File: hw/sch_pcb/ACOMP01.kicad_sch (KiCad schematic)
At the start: 20 parts, among them IC1 TLV3604DCKR, IC2 LMH7220MK_NOPB, J1 Umin ... Umax, J2 Conn_Coaxial, J3 Conn_Coaxial, J4 Conn_Coaxial, J5 Conn_Coaxial, J6 HEADER_2x04_PARALLEL, J7 HEADER_2x04_PARALLEL, M1 HOLE M3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

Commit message: pcb layout
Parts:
- C2: value 100nF -> 1uF
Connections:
- net OUT+_LMH renamed LMH_OUT+
- net OUT+_TLV renamed TLV_OUT+
- net OUT-_LMH renamed LMH_OUT-
- net OUT-_TLV renamed TLV_OUT-
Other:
- note added: "2.4 - 5.5 V"
- note added: "2.7 - 12 V"
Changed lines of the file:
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@@
+    (effects (font (size 1.524 1.524)) (justify left bottom))
+  )
+  (text "2.4 - 5.5 V" (at 102.87 81.28 0)
     (effects (font (size 1.524 1.524)) (justify left bottom))
   )
@@
     (effects (font (size 1.524 1.524)) (justify left bottom))
   )
-  (label "OUT+_TLV" (at 163.83 68.58 180)
+  (text "2.7 - 12 V" (at 102.87 115.57 0)
+    (effects (font (size 1.524 1.524)) (justify left bottom))
+  )
+  (label "IN+_LMH" (at 52.07 106.68 0)
+    (effects (font (size 1.524 1.524)) (justify left bottom))
+  )
+  (label "LMH_OUT+" (at 163.83 100.33 180)
     (effects (font (size 1.524 1.524)) (justify right bottom))
   )
-  (label "OUT-_TLV" (at 129.54 68.58 0)
-    (effects (font (size 1.524 1.524)) (justify left bottom))
-  )
-  (label "IN+_LMH" (at 52.07 106.68 0)
-    (effects (font (size 1.524 1.524)) (justify left bottom))
-  )
   (label "IN+_TLV" (at 52.07 58.42 0)
     (effects (font (size 1.524 1.524)) (justify left bottom))
-  )
-  (label "OUT-_LMH" (at 163.83 113.03 180)
-    (effects (font (size 1.524 1.524)) (justify right bottom))
   )
   (label "IN-_TLV" (at 129.54 77.47 0)
@@
     (effects (font (size 1.524 1.524)) (justify right bottom))
   )
-  (label "OUT-_TLV" (at 163.83 81.28 180)
+  (label "IN-_TLV" (at 52.07 74.93 0)
+    (effects (font (size 1.524 1.524)) (justify left bottom))
+  )
+  (label "LMH_OUT-" (at 163.83 113.03 180)
     (effects (font (size 1.524 1.524)) (justify right bottom))
   )
-  (label "IN-_TLV" (at 52.07 74.93 0)
-    (effects (font (size 1.524 1.524)) (justify left bottom))
-  )
-  (label "OUT+_LMH" (at 128.27 113.03 0)
-    (effects (font (size 1.524 1.524)) (justify left bottom))
-  )
-  (label "OUT-_LMH" (at 90.17 113.03 180)
-    (effects (font (size 1.524 1.524)) (justify right bottom))
+  (label "LMH_OUT+" (at 128.27 113.03 0)
+    (effects (font (size 1.524 1.524)) (justify left bottom))
   )
   (label "IN-_LMH" (at 52.07 123.19 0)
     (effects (font (size 1.524 1.524)) (justify left bottom))
-  )
-  (label "OUT+_TLV" (at 88.9 68.58 180)
-    (effects (font (size 1.524 1.524)) (justify right bottom))
   )
   (label "IN+_LMH" (at 128.27 105.41 0)
@@
     (effects (font (size 1.524 1.524)) (justify right bottom))
   )
-  (label "OUT+_LMH" (at 163.83 100.33 180)
+  (label "TLV_OUT+" (at 88.9 68.58 180)
     (effects (font (size 1.524 1.524)) (justify right bottom))
+  )
+  (label "TLV_OUT-" (at 163.83 81.28 180)
+    (effects (font (size 1.524 1.524)) (justify right bottom))
+  )
+  (label "TLV_OUT+" (at 163.83 68.58 180)
+    (effects (font (size 1.524 1.524)) (justify right bottom))
+  )
+  (label "LMH_OUT-" (at 90.17 113.03 180)
+    (effects (font (size 1.524 1.524)) (justify right bottom))
+  )
+  (label "TLV_OUT-" (at 129.54 68.58 0)
+    (effects (font (size 1.524 1.524)) (justify left bottom))
   )
   (symbol (lib_id "header:HEADER_2x03_PARALLEL") (at 267.97 26.67 0) (unit 1)
@@
       (effects (font (size 1.27 1.27)) (justify left))
     )
-    (property "Value" "100nF" (id 1) (at 246.38 34.29 0)
+    (property "Value" "1uF" (id 1) (at 246.38 34.29 0)
       (effects (font (size 1.27 1.27)) (justify left))
     )
@@
     )
     (path "/7fab2e4e-c967-46aa-8b62-a4eb722fba85"
-      (reference "C2") (unit 1) (value "100nF") (footprint "Capacitor_SMD:C_0805_2012Metric")
+      (reference "C2") (unit 1) (value "1uF") (footprint "Capacitor_SMD:C_0805_2012Metric")
     )
     (path "/f66f54fb-1d0d-47f4-b95c-230a639b65a5"

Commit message: Cleanup of some DRC errors.
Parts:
- J1: value Umin ... Umax -> 2,4 - 5,5V
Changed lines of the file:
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@@
       (effects (font (size 1.524 1.524)))
     )
-    (property "Value" "Umin ... Umax" (id 1) (at 267.97 21.59 0)
+    (property "Value" "2,4 - 5,5V" (id 1) (at 267.97 21.59 0)
       (effects (font (size 1.524 1.524)))
     )
@@
     )
     (path "/00000000-0000-0000-0000-0000549d65bc"
-      (reference "J1") (unit 1) (value "Umin ... Umax") (footprint "Mlab_Pin_Headers:Straight_2x03")
+      (reference "J1") (unit 1) (value "2,4 - 5,5V") (footprint "Mlab_Pin_Headers:Straight_2x03")
     )
     (path "/b19fad9a-d3d5-4b48-b6c5-b8fa621dea36"

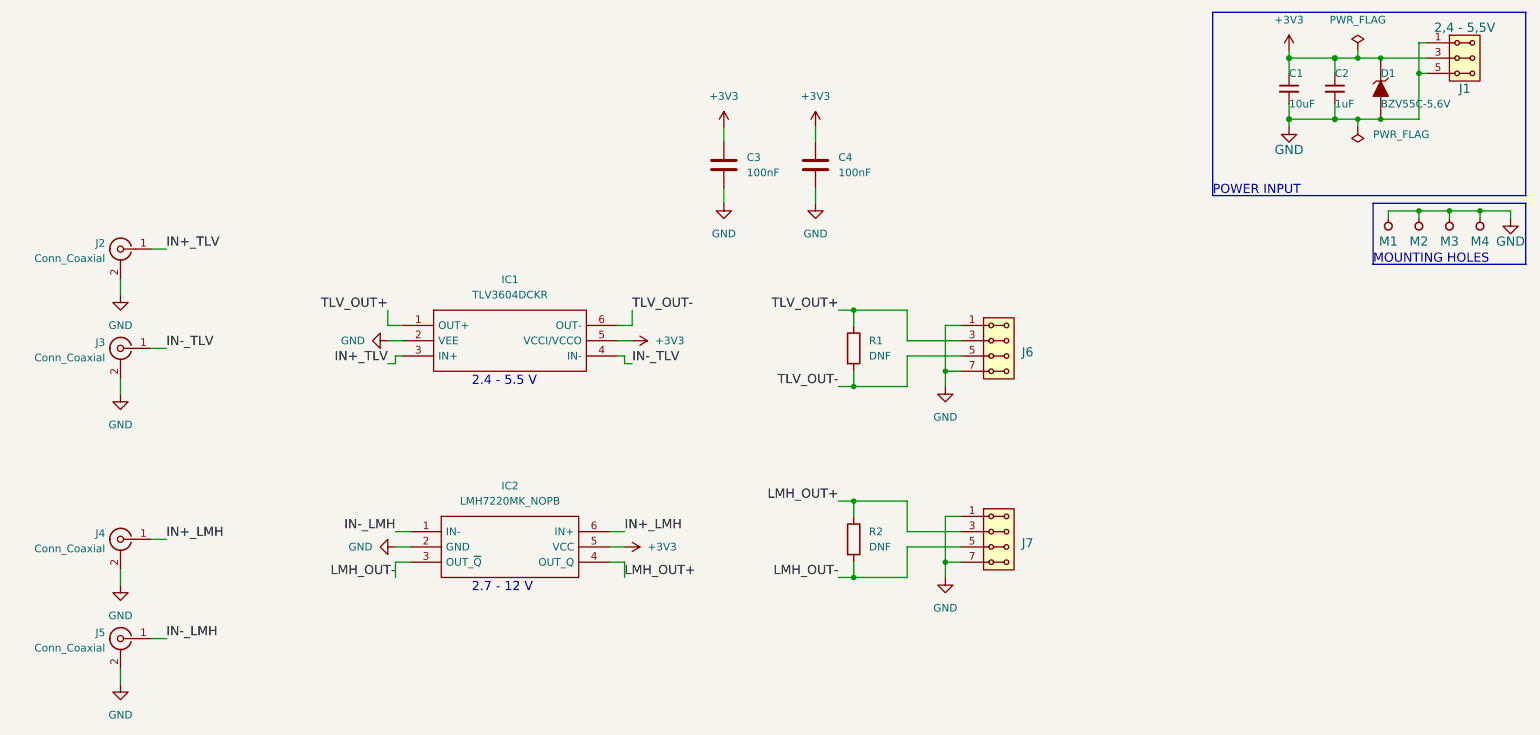
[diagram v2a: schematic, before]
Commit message: Update project to KiCADv9. Resolved #1
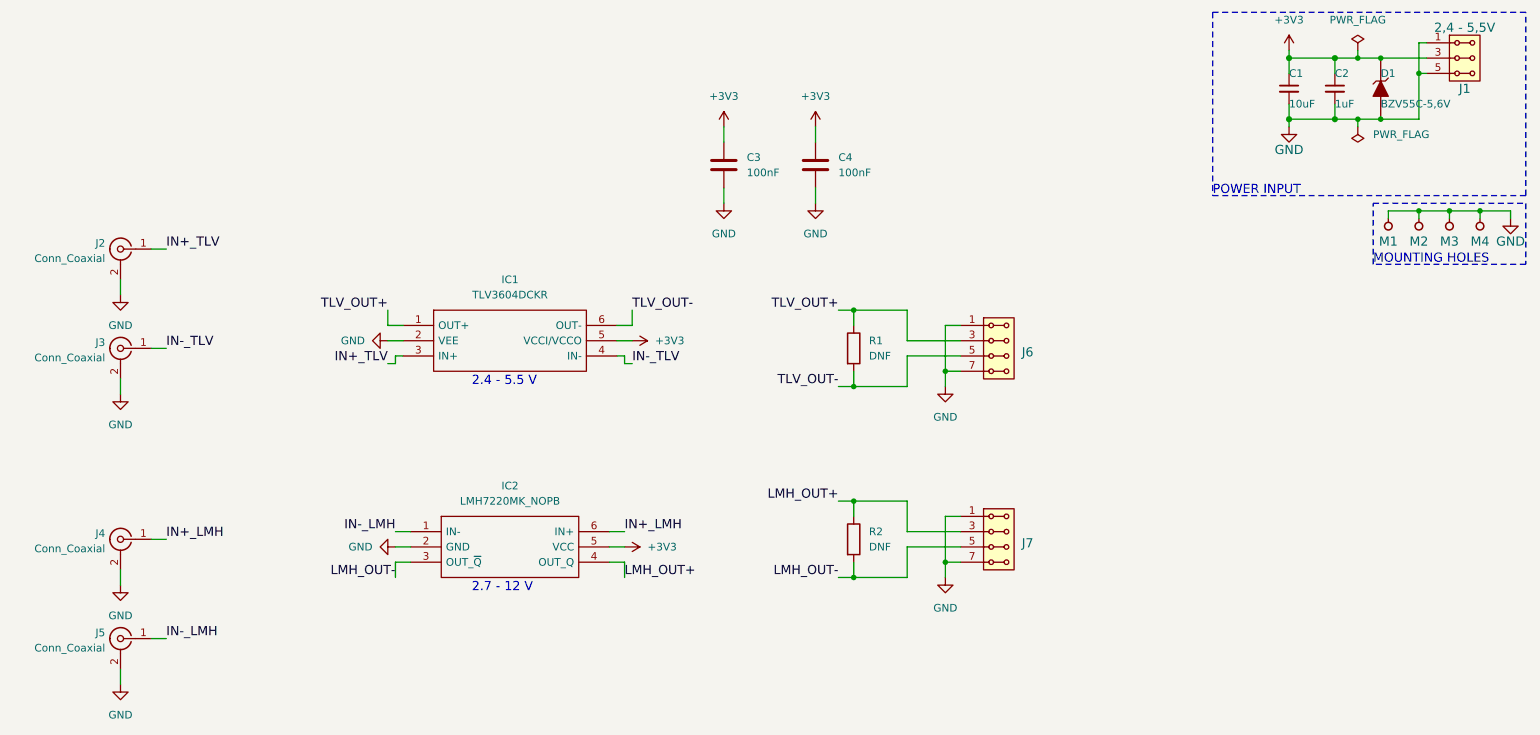
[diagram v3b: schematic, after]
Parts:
- IC1: footprint Mlab_IO:SC-70-6 -> Package_TO_SOT_SMD:SOT-363_SC-70-6
- IC2: footprint Mlab_IO:SOT-23-6 -> Package_TO_SOT_SMD:SOT-23-6
